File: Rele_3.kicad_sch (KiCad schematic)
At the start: 5 parts

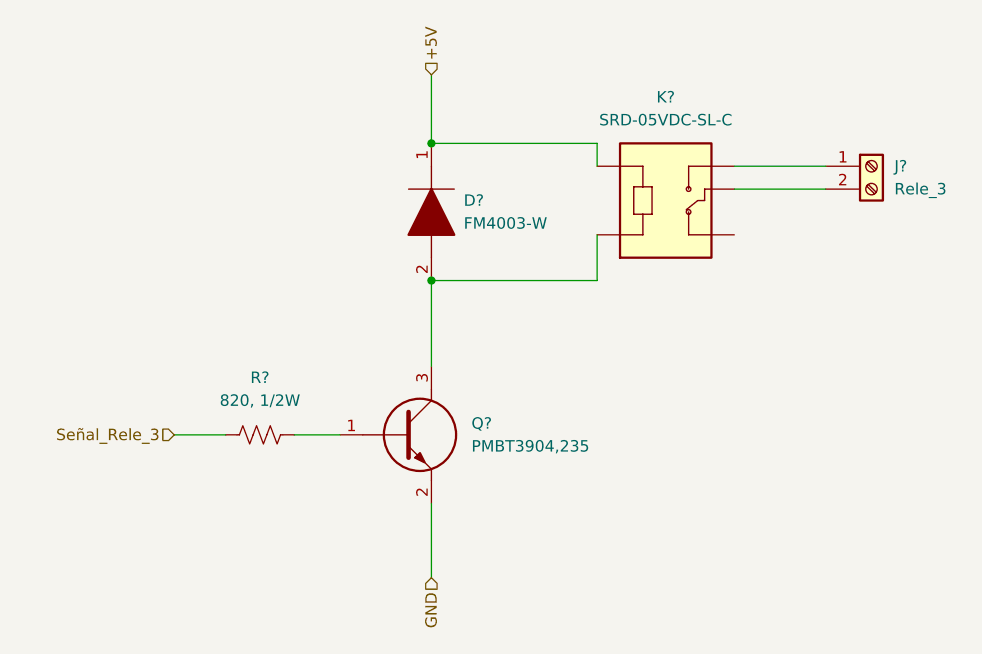
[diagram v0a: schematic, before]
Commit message: Ajuste del esquematico
Se cambio el integrado ESP32 por 2 tiras de pines de 1x15, se quitaron los switches EN y BOOT que ya estan en el NodeMCU, se quito el mutliplexor 74HC y se cablearon las I/O
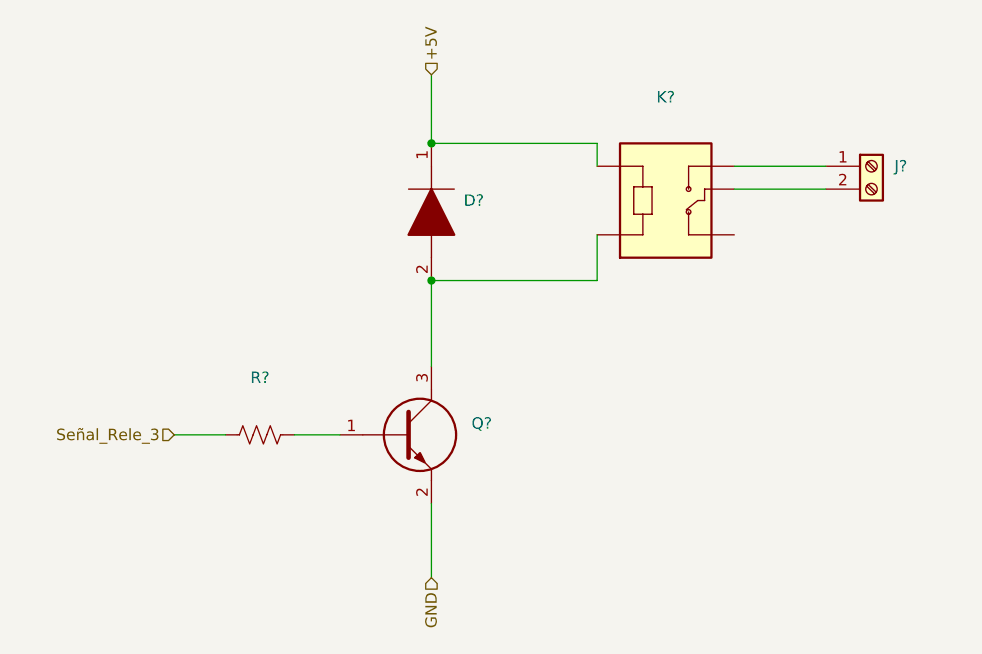
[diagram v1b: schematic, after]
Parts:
- D?: value FM4003-W -> (none); footprint DIOM5025X231N -> (none)
- J?: value Rele_3 -> (none)
- K?: value SRD-05VDC-SL-C -> (none); footprint RELAY_SRD-05VDC-SL-C -> (none)
- Q?: value PMBT3904,235 -> (none); footprint SOT95P230X110-3N -> (none)
- R?: value 820, 1/2W -> (none)
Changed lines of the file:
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@@
     (in_bom yes) (on_board yes) (fields_autoplaced)
     (property "Reference" "R?" (id 0) (at 123.825 99.695 90))
-    (property "Value" "820, 1/2W" (id 1) (at 123.825 102.235 90))
+    (property "Value" "" (id 1) (at 123.825 102.235 90))
     (property "Footprint" "" (id 2) (at 124.079 105.029 90)
       (effects (font (size 1.27 1.27)) hide)
@@
       (effects (font (size 1.27 1.27)) (justify left))
     )
-    (property "Value" "PMBT3904,235" (id 1) (at 147.32 107.3149 0)
+    (property "Value" "" (id 1) (at 147.32 107.3149 0)
       (effects (font (size 1.27 1.27)) (justify left))
     )
-    (property "Footprint" "SOT95P230X110-3N" (id 2) (at 146.685 109.855 0)
+    (property "Footprint" "" (id 2) (at 146.685 109.855 0)
       (effects (font (size 1.27 1.27)) (justify left) hide)
     )
@@
       (effects (font (size 1.27 1.27)) (justify left))
     )
-    (property "Value" "FM4003-W" (id 1) (at 146.4564 82.5499 90)
+    (property "Value" "" (id 1) (at 146.4564 82.5499 90)
       (effects (font (size 1.27 1.27)) (justify left))
     )
-    (property "Footprint" "DIOM5025X231N" (id 2) (at 142.875 85.09 0)
+    (property "Footprint" "" (id 2) (at 142.875 85.09 0)
       (effects (font (size 1.27 1.27)) (justify left) hide)
     )
@@
       (effects (font (size 1.27 1.27)) (justify left))
     )
-    (property "Value" "Rele_3" (id 1) (at 194.31 78.7399 0)
+    (property "Value" "" (id 1) (at 194.31 78.7399 0)
       (effects (font (size 1.27 1.27)) (justify left))
     )
@@
     (in_bom yes) (on_board yes) (fields_autoplaced)
     (property "Reference" "K?" (id 0) (at 168.91 68.5292 0))
-    (property "Value" "SRD-05VDC-SL-C" (id 1) (at 168.91 71.0692 0))
-    (property "Footprint" "RELAY_SRD-05VDC-SL-C" (id 2) (at 168.91 78.74 0)
+    (property "Value" "" (id 1) (at 168.91 71.0692 0))
+    (property "Footprint" "" (id 2) (at 168.91 78.74 0)
       (effects (font (size 1.27 1.27)) (justify left bottom) hide)
     )

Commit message: Modificación de posición de circ. filtrado y circ. de adaptación de tensión
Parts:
- D?, J?, K?, Q?, R?: value (none) -> ~
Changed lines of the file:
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@@
     (in_bom yes) (on_board yes) (fields_autoplaced)
     (property "Reference" "R?" (id 0) (at 123.825 99.695 90))
-    (property "Value" "" (id 1) (at 123.825 102.235 90))
+    (property "Value" "~" (id 1) (at 123.825 102.235 90))
     (property "Footprint" "" (id 2) (at 124.079 105.029 90)
       (effects (font (size 1.27 1.27)) hide)
@@
       (effects (font (size 1.27 1.27)) (justify left))
     )
-    (property "Value" "" (id 1) (at 147.32 107.3149 0)
+    (property "Value" "~" (id 1) (at 147.32 107.3149 0)
       (effects (font (size 1.27 1.27)) (justify left))
     )
@@
       (effects (font (size 1.27 1.27)) (justify left))
     )
-    (property "Value" "" (id 1) (at 146.4564 82.5499 90)
+    (property "Value" "~" (id 1) (at 146.4564 82.5499 90)
       (effects (font (size 1.27 1.27)) (justify left))
     )
@@
       (effects (font (size 1.27 1.27)) (justify left))
     )
-    (property "Value" "" (id 1) (at 194.31 78.7399 0)
+    (property "Value" "~" (id 1) (at 194.31 78.7399 0)
       (effects (font (size 1.27 1.27)) (justify left))
     )
@@
     (in_bom yes) (on_board yes) (fields_autoplaced)
     (property "Reference" "K?" (id 0) (at 168.91 68.5292 0))
-    (property "Value" "" (id 1) (at 168.91 71.0692 0))
+    (property "Value" "~" (id 1) (at 168.91 71.0692 0))
     (property "Footprint" "" (id 2) (at 168.91 78.74 0)
       (effects (font (size 1.27 1.27)) (justify left bottom) hide)

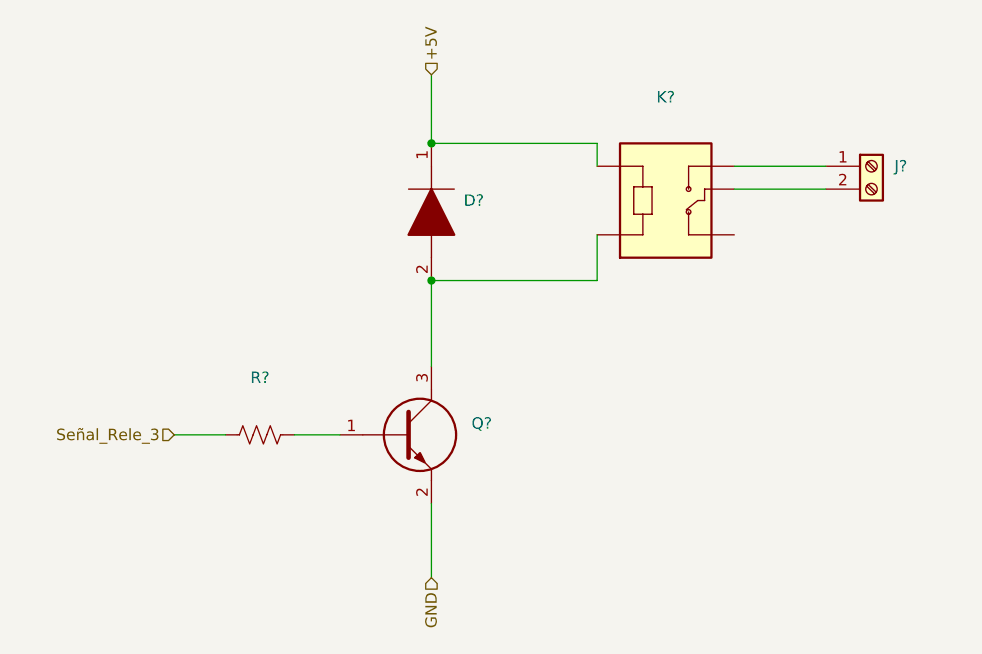
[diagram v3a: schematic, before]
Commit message: Actualización de SCH según placa industrial, y búsqueda de footprints.
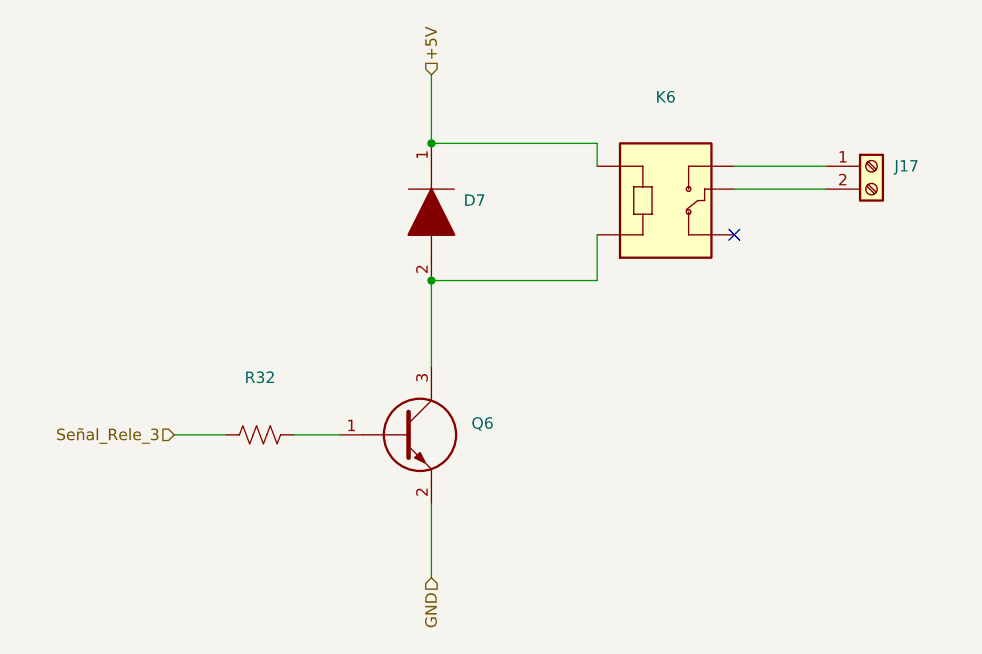
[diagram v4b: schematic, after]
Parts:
- D7: renamed from D?; value ~ -> (none)
- J17: renamed from J?; value ~ -> (none)
- K6: renamed from K?; value ~ -> (none)
- Q6: renamed from Q?; value ~ -> (none)
- R32: renamed from R?; value ~ -> (none)
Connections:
- no-connect marks 0 -> 1
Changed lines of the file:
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@@
   (junction (at 142.875 88.9) (diameter 0) (color 0 0 0 0)
   )
+  (no_connect (at 176.53 83.82))
   (wire (pts (xy 127.635 106.045) (xy 132.715 106.045))
     (stroke (width 0) (type default) (color 0 0 0 0))
@@
   (symbol (lib_id "Device:R_US") (at 123.825 106.045 90) (unit 1)
     (in_bom yes) (on_board yes) (fields_autoplaced)
-    (property "Reference" "R?" (id 0) (at 123.825 99.695 90))
-    (property "Value" "~" (id 1) (at 123.825 102.235 90))
+    (property "Reference" "R32" (id 0) (at 123.825 99.695 90))
+    (property "Value" "" (id 1) (at 123.825 102.235 90))
     (property "Footprint" "" (id 2) (at 124.079 105.029 90)
       (effects (font (size 1.27 1.27)) hide)
@@
   (symbol (lib_id "PMBT3904,235:PMBT3904,235") (at 132.715 106.045 0) (unit 1)
     (in_bom yes) (on_board yes) (fields_autoplaced)
-    (property "Reference" "Q?" (id 0) (at 147.32 104.7749 0)
+    (property "Reference" "Q6" (id 0) (at 147.32 104.7749 0)
       (effects (font (size 1.27 1.27)) (justify left))
     )
-    (property "Value" "~" (id 1) (at 147.32 107.3149 0)
+    (property "Value" "" (id 1) (at 147.32 107.3149 0)
       (effects (font (size 1.27 1.27)) (justify left))
     )
@@
   (symbol (lib_id "FM4003-W:FM4003-W") (at 142.875 73.66 270) (unit 1)
     (in_bom yes) (on_board yes) (fields_autoplaced)
-    (property "Reference" "D?" (id 0) (at 146.4564 80.0099 90)
+    (property "Reference" "D7" (id 0) (at 146.4564 80.0099 90)
       (effects (font (size 1.27 1.27)) (justify left))
     )
-    (property "Value" "~" (id 1) (at 146.4564 82.5499 90)
+    (property "Value" "" (id 1) (at 146.4564 82.5499 90)
       (effects (font (size 1.27 1.27)) (justify left))
     )
@@
   (symbol (lib_id "Connector:Screw_Terminal_01x02") (at 191.77 76.2 0) (unit 1)
     (in_bom yes) (on_board yes) (fields_autoplaced)
-    (property "Reference" "J?" (id 0) (at 194.31 76.1999 0)
+    (property "Reference" "J17" (id 0) (at 194.31 76.1999 0)
       (effects (font (size 1.27 1.27)) (justify left))
     )
-    (property "Value" "~" (id 1) (at 194.31 78.7399 0)
+    (property "Value" "" (id 1) (at 194.31 78.7399 0)
       (effects (font (size 1.27 1.27)) (justify left))
     )
@@
   (symbol (lib_id "SRD-05VDC-SL-C:SRD-05VDC-SL-C") (at 168.91 78.74 0) (unit 1)
     (in_bom yes) (on_board yes) (fields_autoplaced)
-    (property "Reference" "K?" (id 0) (at 168.91 68.5292 0))
-    (property "Value" "~" (id 1) (at 168.91 71.0692 0))
+    (property "Reference" "K6" (id 0) (at 168.91 68.5292 0))
+    (property "Value" "" (id 1) (at 168.91 71.0692 0))
     (property "Footprint" "" (id 2) (at 168.91 78.74 0)
       (effects (font (size 1.27 1.27)) (justify left bottom) hide)

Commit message: Fin de SCH, config de inicio para PCB
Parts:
- D7: value (none) -> FM4003-W; footprint (none) -> FM4003W:DIOM5025X231N
- J17: value (none) -> Rele_3; footprint (none) -> TB002-500-02BE:TB00250002BE
- K6: value (none) -> SRD-05VDC-SL-C; footprint (none) -> SRD-05VDC-SL-C-Version_2:RELAY_SRD-05VDC-SL-C
- Q6: value (none) -> PMBT3904,235; footprint (none) -> PMBT3904,235:SOT95P230X110-3N
- R32: value (none) -> 820, 1/2W; footprint (none) -> Resistor_SMD:R_0805_2012Metric
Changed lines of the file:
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@@
     (in_bom yes) (on_board yes) (fields_autoplaced)
     (property "Reference" "R32" (id 0) (at 123.825 99.695 90))
-    (property "Value" "" (id 1) (at 123.825 102.235 90))
-    (property "Footprint" "" (id 2) (at 124.079 105.029 90)
+    (property "Value" "820, 1/2W" (id 1) (at 123.825 102.235 90))
+    (property "Footprint" "Resistor_SMD:R_0805_2012Metric" (id 2) (at 124.079 105.029 90)
       (effects (font (size 1.27 1.27)) hide)
     )
@@
       (effects (font (size 1.27 1.27)) (justify left))
     )
-    (property "Value" "" (id 1) (at 147.32 107.3149 0)
+    (property "Value" "PMBT3904,235" (id 1) (at 147.32 107.3149 0)
       (effects (font (size 1.27 1.27)) (justify left))
     )
-    (property "Footprint" "" (id 2) (at 146.685 109.855 0)
+    (property "Footprint" "PMBT3904,235:SOT95P230X110-3N" (id 2) (at 146.685 109.855 0)
       (effects (font (size 1.27 1.27)) (justify left) hide)
     )
@@
       (effects (font (size 1.27 1.27)) (justify left))
     )
-    (property "Value" "" (id 1) (at 146.4564 82.5499 90)
+    (property "Value" "FM4003-W" (id 1) (at 146.4564 82.5499 90)
       (effects (font (size 1.27 1.27)) (justify left))
     )
-    (property "Footprint" "" (id 2) (at 142.875 85.09 0)
+    (property "Footprint" "FM4003W:DIOM5025X231N" (id 2) (at 142.875 85.09 0)
       (effects (font (size 1.27 1.27)) (justify left) hide)
     )
@@
       (effects (font (size 1.27 1.27)) (justify left))
     )
-    (property "Value" "" (id 1) (at 194.31 78.7399 0)
+    (property "Value" "Rele_3" (id 1) (at 194.31 78.7399 0)
       (effects (font (size 1.27 1.27)) (justify left))
     )
-    (property "Footprint" "" (id 2) (at 191.77 76.2 0)
+    (property "Footprint" "TB002-500-02BE:TB00250002BE" (id 2) (at 191.77 76.2 0)
       (effects (font (size 1.27 1.27)) hide)
     )
@@
     (in_bom yes) (on_board yes) (fields_autoplaced)
     (property "Reference" "K6" (id 0) (at 168.91 68.5292 0))
-    (property "Value" "" (id 1) (at 168.91 71.0692 0))
-    (property "Footprint" "" (id 2) (at 168.91 78.74 0)
+    (property "Value" "SRD-05VDC-SL-C" (id 1) (at 168.91 71.0692 0))
+    (property "Footprint" "SRD-05VDC-SL-C-Version_2:RELAY_SRD-05VDC-SL-C" (id 2) (at 168.91 78.74 0)
       (effects (font (size 1.27 1.27)) (justify left bottom) hide)
     )

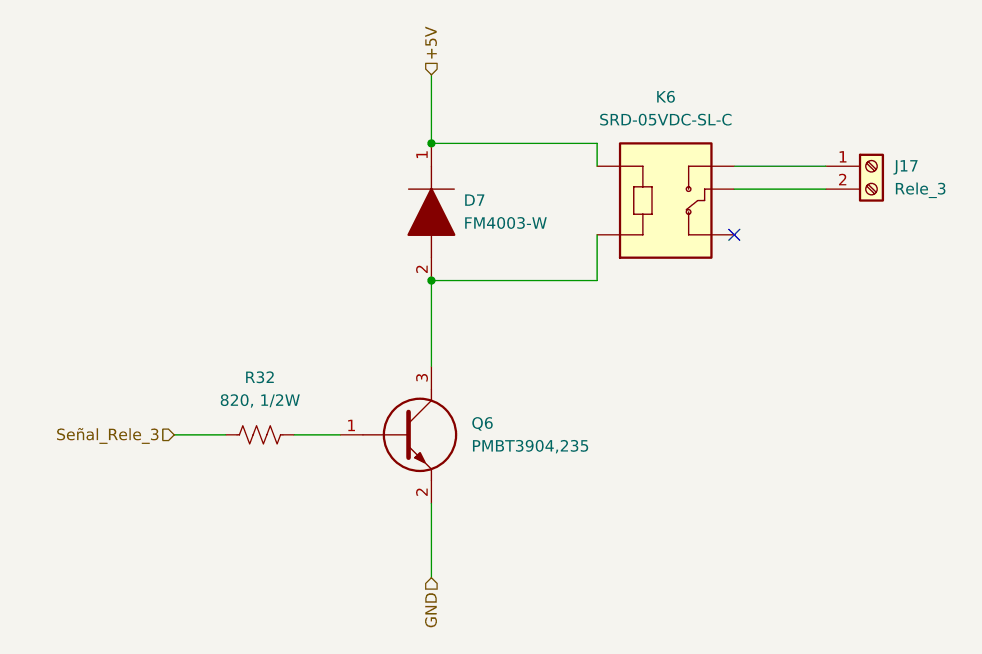
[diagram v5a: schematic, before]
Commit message: Cambios en SCH y PCB.
Se cambio el adaptador de nivel 5-3,3V por un circuito con MOSFET 2N7002, dado que ya no hay stock del NXB. Se modificó el footprint del expansor I/O por uno thorugh-hole.
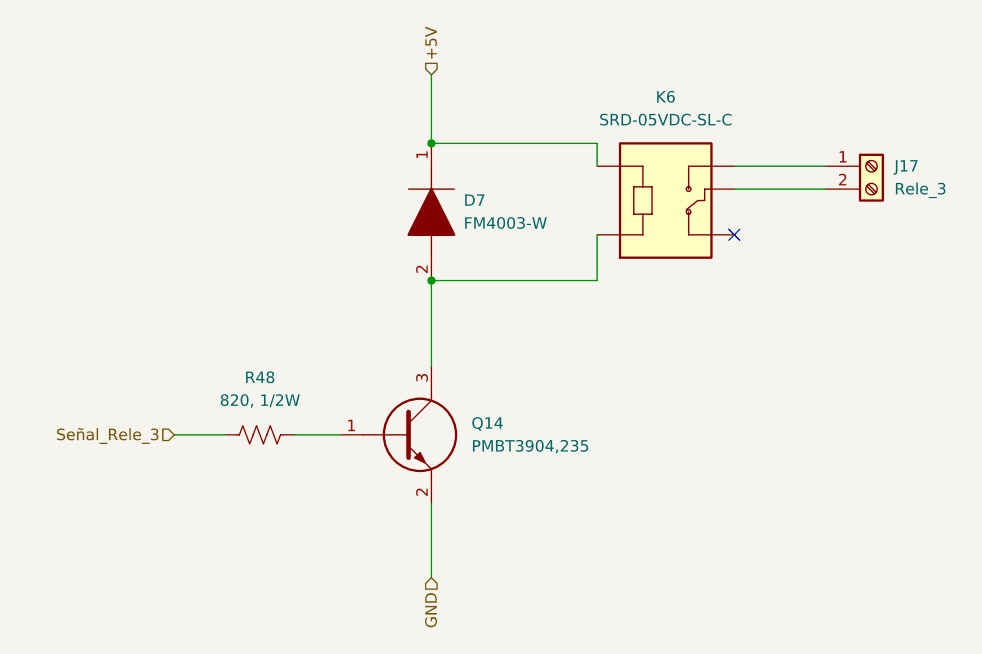
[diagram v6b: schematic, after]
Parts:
- renumbered Q6 to Q14, R32 to R48
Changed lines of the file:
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@@
   (symbol (lib_id "Device:R_US") (at 123.825 106.045 90) (unit 1)
     (in_bom yes) (on_board yes) (fields_autoplaced)
-    (property "Reference" "R32" (id 0) (at 123.825 99.695 90))
+    (property "Reference" "R48" (id 0) (at 123.825 99.695 90))
     (property "Value" "820, 1/2W" (id 1) (at 123.825 102.235 90))
     (property "Footprint" "Resistor_SMD:R_0805_2012Metric" (id 2) (at 124.079 105.029 90)
@@
   (symbol (lib_id "PMBT3904,235:PMBT3904,235") (at 132.715 106.045 0) (unit 1)
     (in_bom yes) (on_board yes) (fields_autoplaced)
-    (property "Reference" "Q6" (id 0) (at 147.32 104.7749 0)
+    (property "Reference" "Q14" (id 0) (at 147.32 104.7749 0)
       (effects (font (size 1.27 1.27)) (justify left))
     )

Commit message: Se finalizó con el PCB del prototipo.
Dado que se buscó a toda costa que el PCB fuera de 1 capa, en varios puntos del circuito se tuvieron que agregar pin headers individuales para conectar a 3V3 y GND, junto con tiras de pin headers. Cada una de estas se conectara luego entre si mediante cables.

Tambien se generaron los archivos Gerber y BOM.
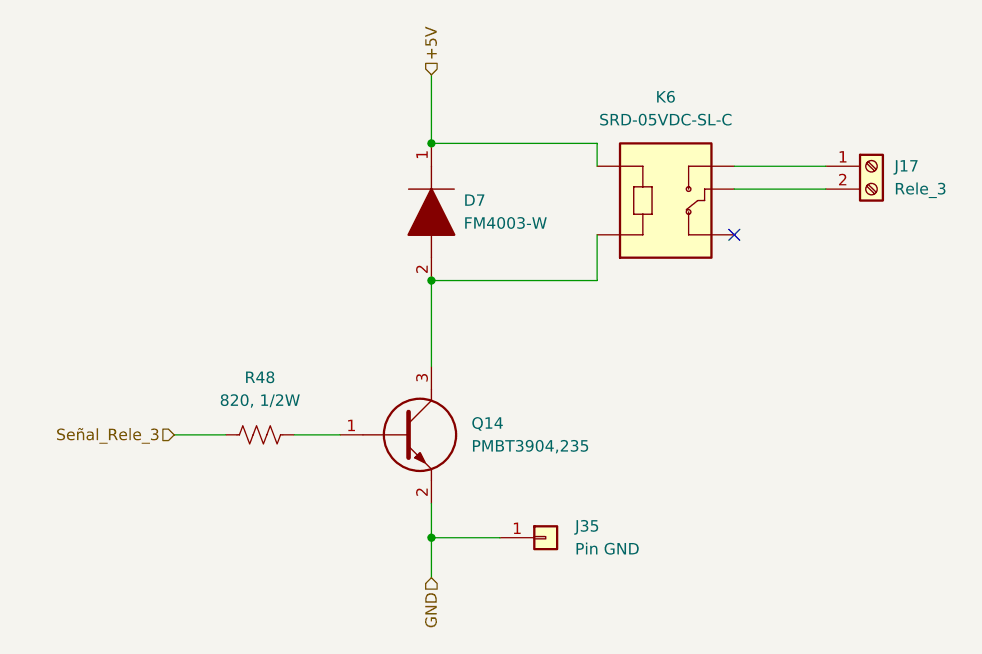
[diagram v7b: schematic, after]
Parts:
- added J35: Pin GND, Connector_PinHeader_2.54mm:PinHeader_1x01_P2.54mm_Vertical, symbol Connector_Generic:Conn_01x01
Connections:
- net GND: now also J35.1 (Pin_1)
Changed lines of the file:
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@@
   (junction (at 142.875 88.9) (diameter 0) (color 0 0 0 0)
+  )
+  (junction (at 142.875 117.475) (diameter 0) (color 0 0 0 0)
   )
   (no_connect (at 176.53 83.82))
@@
     (stroke (width 0) (type default) (color 0 0 0 0))
   )
-  (wire (pts (xy 142.875 113.665) (xy 142.875 121.92))
+  (wire (pts (xy 142.875 117.475) (xy 150.495 117.475))
+    (stroke (width 0) (type default) (color 0 0 0 0))
+  )
+  (wire (pts (xy 142.875 113.665) (xy 142.875 117.475))
     (stroke (width 0) (type default) (color 0 0 0 0))
   )
   (wire (pts (xy 176.53 76.2) (xy 186.69 76.2))
+    (stroke (width 0) (type default) (color 0 0 0 0))
+  )
+  (wire (pts (xy 142.875 117.475) (xy 142.875 121.92))
     (stroke (width 0) (type default) (color 0 0 0 0))
   )
@@
     (pin "2")
   )
+  (symbol (lib_id "Connector_Generic:Conn_01x01") (at 155.575 117.475 0) (unit 1)
+    (in_bom yes) (on_board yes) (fields_autoplaced)
+    (property "Reference" "J35" (id 0) (at 158.8262 116.2049 0)
+      (effects (font (size 1.27 1.27)) (justify left))
+    )
+    (property "Value" "Pin GND" (id 1) (at 158.8262 118.7449 0)
+      (effects (font (size 1.27 1.27)) (justify left))
+    )
+    (property "Footprint" "Connector_PinHeader_2.54mm:PinHeader_1x01_P2.54mm_Vertical" (id 2) (at 155.575 117.475 0)
+      (effects (font (size 1.27 1.27)) hide)
+    )
+    (property "Datasheet" "~" (id 3) (at 155.575 117.475 0)
+      (effects (font (size 1.27 1.27)) hide)
+    )
+    (pin "1")
+  )
   (symbol (lib_id "PMBT3904,235:PMBT3904,235") (at 132.715 106.045 0) (unit 1)
